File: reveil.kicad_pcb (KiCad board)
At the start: 2 copper layers, 170 x 90 mm, 33 parts, among them J1 Barrel_Jack_Switch, J2 AudioJack3_SwitchTR, Q1 2N3904, Q2 IRLB8721PBF, U1 MAX7219, U2 MAX7219

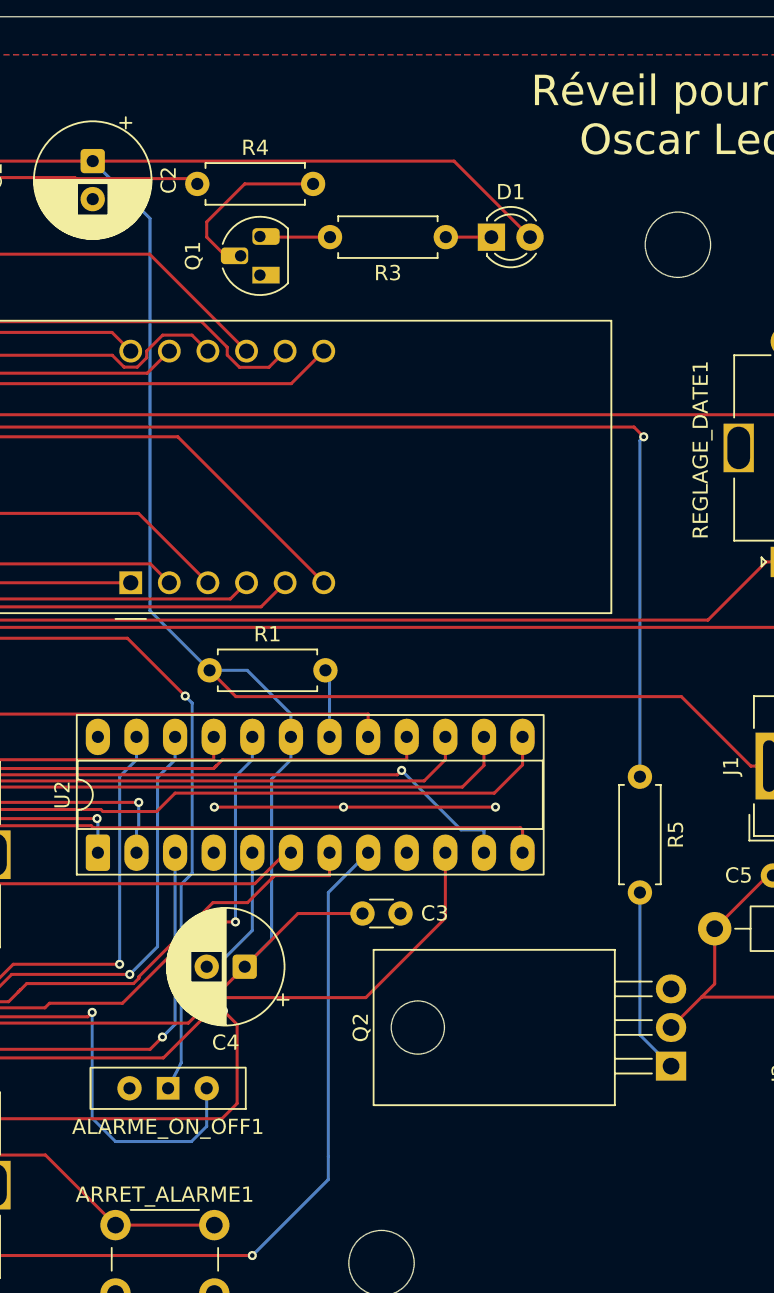
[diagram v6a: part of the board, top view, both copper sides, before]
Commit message: Schéma/PCB : ajoute les pull-down de grille Q2 et de base Q1
GPIO18 est en haute impédance pendant le boot/reset du Pico. Sans rien
pour fixer son potentiel, la grille de Q2 pouvait flotter à un niveau
intermédiaire (vibration intempestive du moteur, ou Q2 à moitié
passant qui chauffe), et la base de Q1 pouvait aussi flotter et le
faire conduire légèrement, ce qui aurait pu repousser du courant vers
la grille de Q2 à travers R5.

Ajoute :
- R6 (100 kΩ) entre la grille et la source de Q2 (donc vers GND,
  Source étant déjà relié à GND)
- R7 (47 kΩ) entre la base et l'émetteur de Q1, pour garder Q1
  déterministement bloqué pendant que sa base flotte

Empreintes placées et pistes routées sur le PCB.

Connectivité vérifiée via le netlist KiCad (R6 sur Net-(Q2-G) avec Q2-G
et R5 ; R7 sur Net-(Q1-B) avec Q1-B et R4 ; R6 et R7 tous deux sur le
net GND avec Q2-S et Q1-E) et ERC/DRC revérifiés via le conteneur
Docker KiBot : 0 erreur/avertissement ERC ; DRC revenu à la référence
(6 avertissements silk_edge_clearance préexistants sur J2), aucun
écart schéma/PCB.

Co-Authored-By: Claude Sonnet 5 <noreply@anthropic.com>
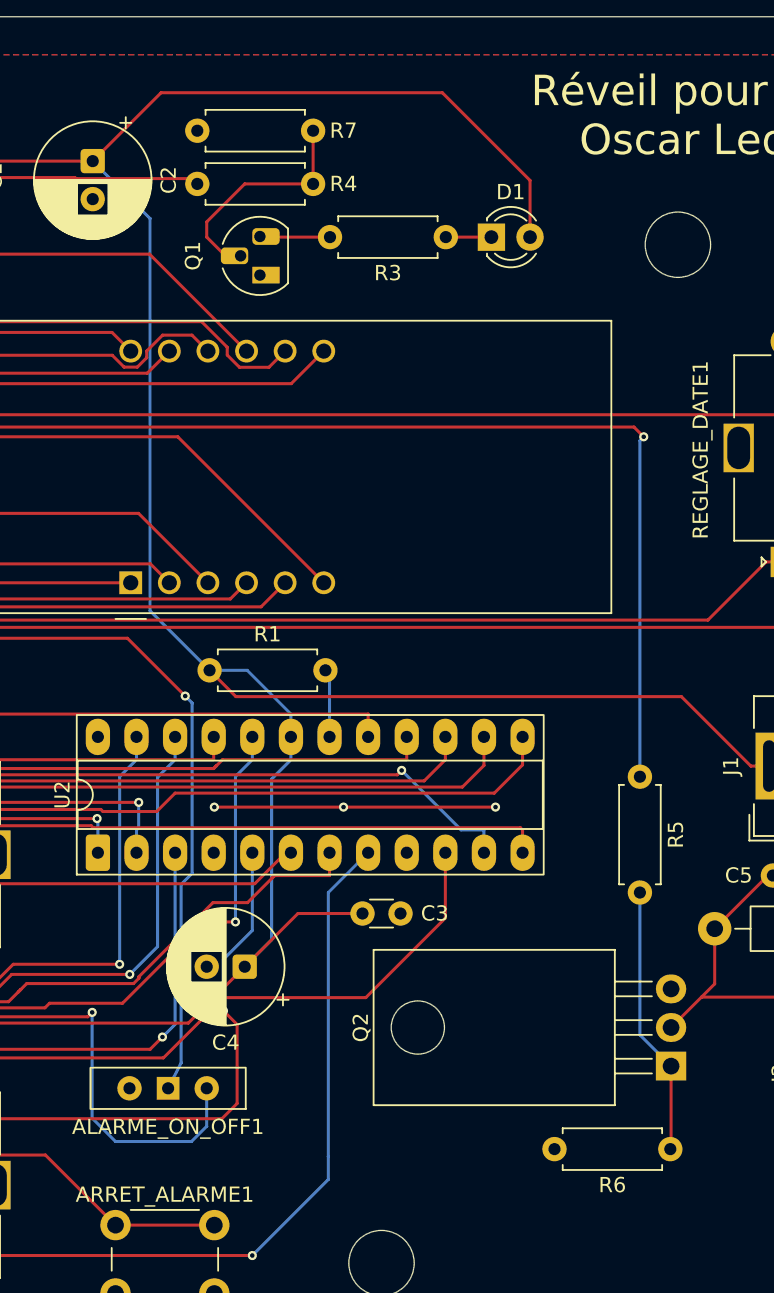
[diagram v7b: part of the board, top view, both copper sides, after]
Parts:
- added R6: 100k, Resistor_THT:R_Axial_DIN0207_L6.3mm_D2.5mm_P7.62mm_Horizontal, F.Cu at (229.5, 94.5)
- added R7: 47K, Resistor_THT:R_Axial_DIN0207_L6.3mm_D2.5mm_P7.62mm_Horizontal, F.Cu at (206.0, 27.5)
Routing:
- net VBUS: track 327.2 -> 333.1 mm
- net Net-(Q2-G): track 12.3 -> 17.7 mm
- net Net-(Q1-B): track 11.8 -> 15.3 mm

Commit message: Schéma/PCB : fixe la valeur de R1 (ISET de U2) à 47 kΩ
R1 avait la valeur placeholder « R » au lieu d'une vraie valeur. C'est
la résistance ISET de U2 (MAX7219 pilotant HEURE/ALARME) : sans valeur
correcte, HEURE/ALARME n'auraient pas la même luminosité que
DATE/ANNEE (pilotés par U1, dont R2 = 47 kΩ).

Aligne R1 sur R2 (47 kΩ, ≈ 14 mA par segment) dans heure_alarme.kicad_sch
et sur le PCB. ERC/DRC revérifiés via le conteneur Docker KiBot :
0 erreur/avertissement ERC, DRC inchangé (6 avertissements
silk_edge_clearance préexistants sur J2).

Co-Authored-By: Claude Sonnet 5 <noreply@anthropic.com>
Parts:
- R1: value R -> 47K
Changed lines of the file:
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@@
 			)
 		)
-		(property "Value" "R"
+		(property "Value" "47K"
 			(at 3.81 2.37 0)
 			(layer "F.Fab")
